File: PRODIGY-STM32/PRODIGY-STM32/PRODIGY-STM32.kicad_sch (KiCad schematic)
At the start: 10 parts

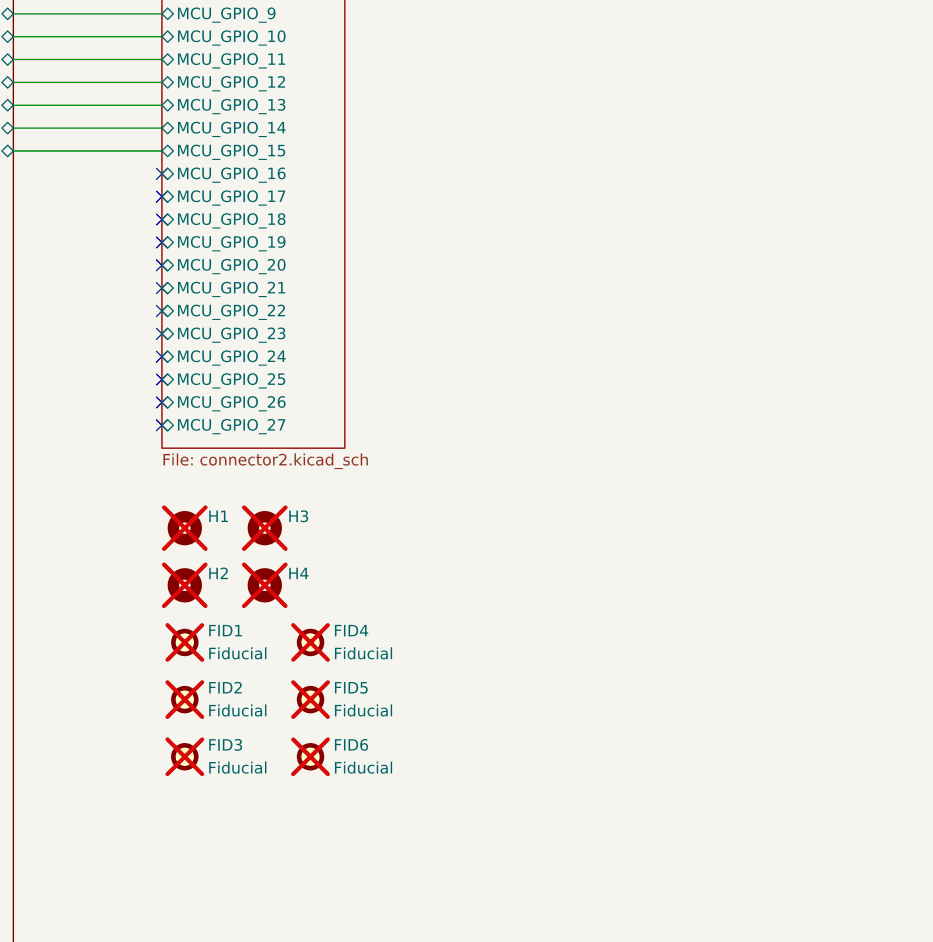
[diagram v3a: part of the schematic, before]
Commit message: ESP32 and ATMEGA bom done.
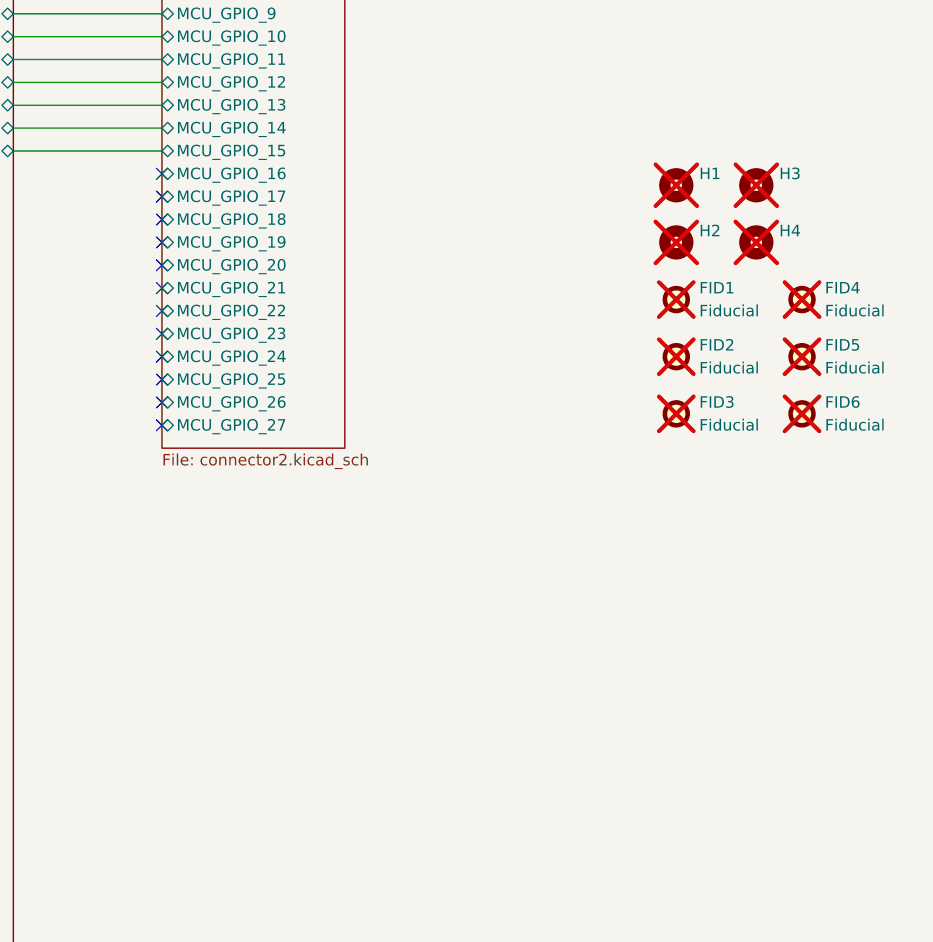
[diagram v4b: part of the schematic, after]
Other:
- moved on the sheet: FID1, FID2, FID3, FID4, FID5, FID6, H1, H2, H3, H4

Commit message: stm32 started, footprints updated, lazout started
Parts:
- H1, H2, H3, H4: footprint MountingHole:MountingHole_3.2mm_M3_ISO14580_Pad -> MountingHole:MountingHole_3.2mm_M3_ISO7380_Pad_TopBottom
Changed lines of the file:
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@@
 			)
 		)
-		(property "Footprint" "MountingHole:MountingHole_3.2mm_M3_ISO14580_Pad"
+		(property "Footprint" "MountingHole:MountingHole_3.2mm_M3_ISO7380_Pad_TopBottom"
 			(at 241.3 87.63 0)
 			(effects
@@
 		)
 		(instances
-			(project ""
+			(project "PRODIGY-STM32"
 				(path "/f2f1c781-b8fe-416b-b7a0-b424640c1d9f"
 					(reference "H1")
@@
 			)
 		)
-		(property "Footprint" "MountingHole:MountingHole_3.2mm_M3_ISO14580_Pad"
+		(property "Footprint" "MountingHole:MountingHole_3.2mm_M3_ISO7380_Pad_TopBottom"
 			(at 250.19 87.63 0)
 			(effects
@@
 			)
 		)
-		(property "Footprint" "MountingHole:MountingHole_3.2mm_M3_ISO14580_Pad"
+		(property "Footprint" "MountingHole:MountingHole_3.2mm_M3_ISO7380_Pad_TopBottom"
 			(at 241.3 93.98 0)
 			(effects
@@
 			)
 		)
-		(property "Footprint" "MountingHole:MountingHole_3.2mm_M3_ISO14580_Pad"
+		(property "Footprint" "MountingHole:MountingHole_3.2mm_M3_ISO7380_Pad_TopBottom"
 			(at 250.19 93.98 0)
 			(effects
@@
 		)
 		(instances
-			(project ""
+			(project "PRODIGY-STM32"
 				(path "/f2f1c781-b8fe-416b-b7a0-b424640c1d9f"
 					(reference "FID1")
